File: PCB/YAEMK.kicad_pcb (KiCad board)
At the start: 2 copper layers, 165.8 x 130.8 mm, 222 parts, among them J1 DBG, P1 PC, P2 Link, P3 SSD1107, Q1 MMUN2133LT1G, Q2 DMMT5401, Q3 AO3401A, SW1 ALPS EC11, U1 24LC64, U2 SSP6206, U3 USBLC6-2SC6, U4 USBLC6-2SC6, U5 STM32F303CCTx

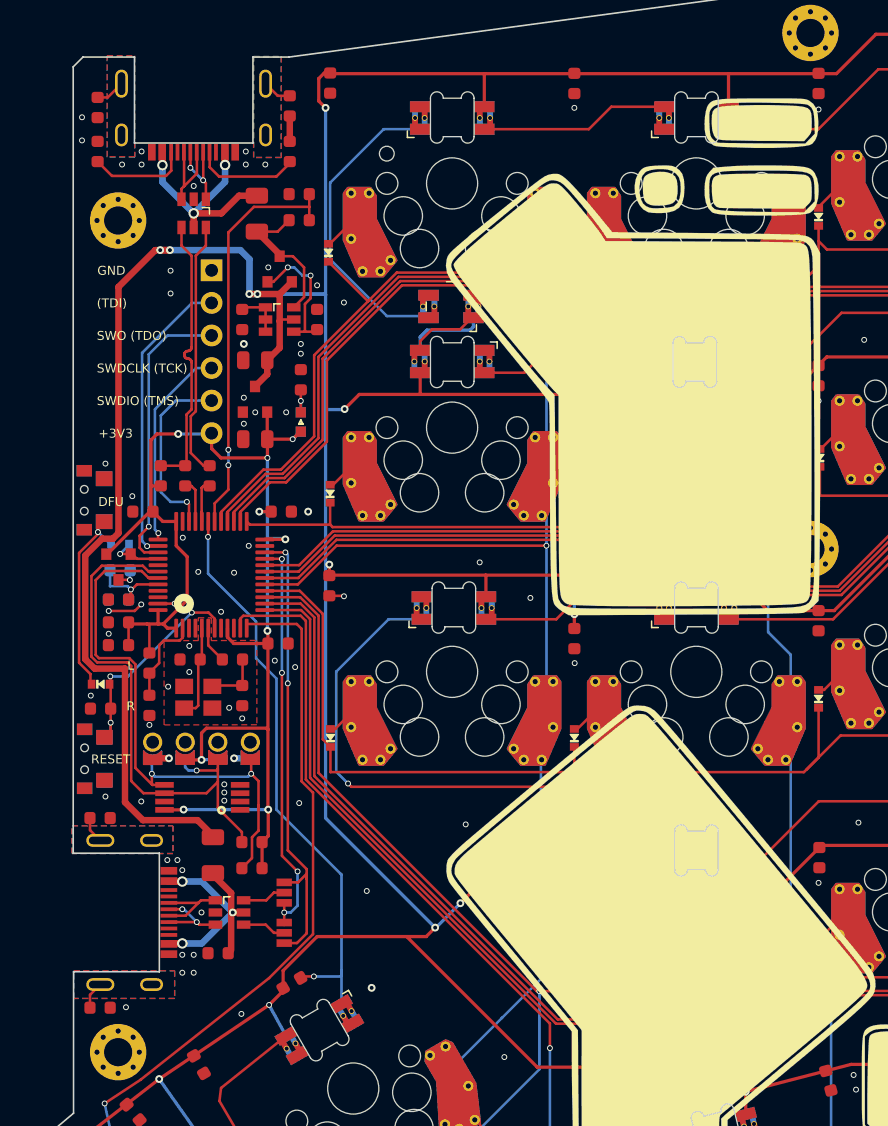
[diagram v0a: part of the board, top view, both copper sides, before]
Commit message: Update Reset / DFU circut to single button version
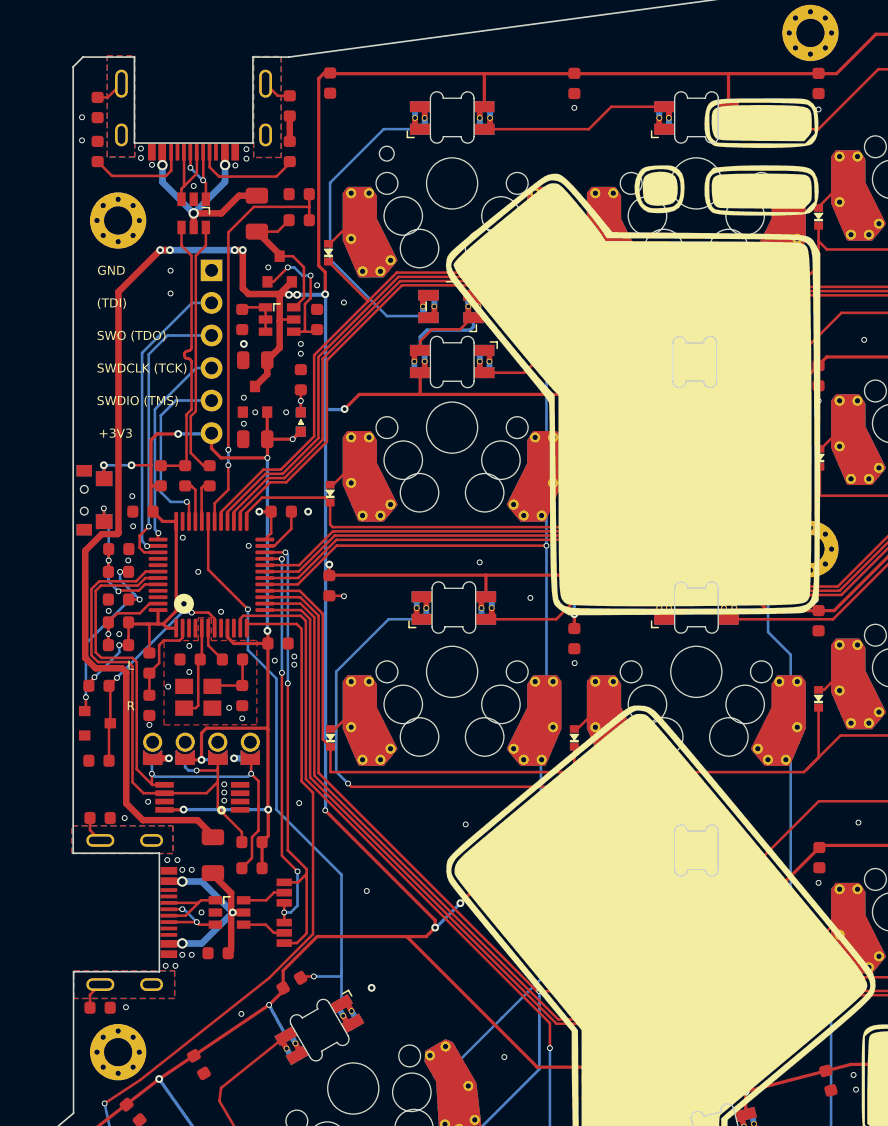
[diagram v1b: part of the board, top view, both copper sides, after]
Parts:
- removed D68, D69: 1N4148, prettylib:D_SOD-523
- removed S33: RESET, prettylib:SMD_Tacticle_Switch_TS24CA_flipable
- added R27: 100k, prettylib:SMD-0603, F.Cu at (80.6, 77.9)
- C40: value 100n -> 10u
- C42: value 100n -> 1u
- Q1: value MMUN2133LT1G -> 2N7002
- R11: value 220 -> 10k; moved to F.Cu
- R14: value 1M -> 10k; moved to F.Cu
- S32: value DFU -> RESET + DFU
- moved C42 12.7 mm to (79.1, 90.4), turned to 180 degrees
- moved Q1 12.3 mm to (79.0, 87.5), turned to 0 degrees
- moved C40 10.8 mm to (80.6, 75.7)
- moved R14 6.90 mm to (79.1, 84.6), turned to 0 degrees
- moved R11 1.65 mm to (80.7, 73.9), turned to 0 degrees
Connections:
- C40 pad 1: VSS -> BOOT0
- C40 pad 2: NRST -> Net-(C40-Pad2)
- C42 pad 1: VSS -> NRST
- C42 pad 2: BOOT0 -> VSS
- Q1 pad 1: BOOT0_CHARGE -> Net-(C40-Pad2)
- Q1 pad 2: VDD -> VSS
- Q1 pad 3: Net-(Q1-Pad3) -> NRST
- R11 pad 1: Net-(Q1-Pad3) -> BOOT0
- R11 pad 2: BOOT0 -> VSS
- R14 pad 1: BOOT0 -> VDD
- R14 pad 2: VSS -> NRST
- S32 pad 1: Net-(D68-Pad1) -> BOOT0
- S32 pad 2: VSS -> VDD
- U5 pad 40: BOOT0_CHARGE -> (no net)
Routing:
- net Net-(D68-Pad1): track 16.6 -> 0.00 mm, vias 1 -> 0
- net Net-(C40-Pad2): track 0.00 -> 15.0 mm, vias 0 -> 3
- net BOOT0: track 6.79 -> 16.3 mm, vias 1 -> 3
- net VSS: track 14.5 -> 19.9 mm
- net VDD: track 110.0 -> 114.3 mm, vias 9 -> 12
- net BOOT0_CHARGE: track 4.22 -> 0.00 mm, vias 1 -> 0
- net RGB_VDD: track 1003.6 -> 1000.7 mm, vias 29 -> 32
- net Net-(Q1-Pad3): track 1.54 -> 0.00 mm, vias 1 -> 0
- net Row2: track 153.4 -> 154.6 mm
- net I2C1_SCL: track 42.5 -> 41.5 mm
- net I2C1_SDA: track 45.1 -> 44.1 mm
- net NRST: track 17.3 -> 17.5 mm, vias 3 -> 2
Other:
- board text removed: "DFU"
- board text removed: "RESET"

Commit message: Update Gerbers
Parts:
- moved Q1 0.11 mm to (79.1, 87.5)
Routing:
- net VSS: vias 112 -> 114

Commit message: Update Plugdetect Values
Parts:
- R16: value 100k -> 10k
- R22: value 100k -> 47k
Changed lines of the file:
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@@
     (add_net "Net-(F1-Pad1)")
     (add_net "Net-(P1-PadA5)")
+    (add_net "Net-(P1-PadA8)")
     (add_net "Net-(P1-PadB5)")
+    (add_net "Net-(P1-PadB8)")
     (add_net "Net-(P1-PadS1)")
+    (add_net "Net-(P2-PadA5)")
+    (add_net "Net-(P2-PadA8)")
+    (add_net "Net-(P2-PadB5)")
+    (add_net "Net-(P2-PadB8)")
     (add_net "Net-(P2-PadS1)")
     (add_net "Net-(Q2-Pad1)")
@@
     (add_net "Net-(R18-Pad2)")
     (add_net "Net-(R19-Pad2)")
+    (add_net "Net-(U5-Pad10)")
+    (add_net "Net-(U5-Pad3)")
+    (add_net "Net-(U5-Pad4)")
+    (add_net "Net-(U5-Pad40)")
+    (add_net "Net-(U5-Pad41)")
+    (add_net "Net-(U5-Pad45)")
+    (add_net "Net-(U5-Pad46)")
     (add_net PLUG_DETECT)
     (add_net RGB_DATA)
@@
       (effects (font (size 1 1) (thickness 0.15)))
     )
-    (fp_text value 100k (at 0 1.43 90) (layer F.Fab) hide
+    (fp_text value 10k (at 0 1.43 90) (layer F.Fab) hide
       (effects (font (size 1 1) (thickness 0.15)))
     )
@@
       (effects (font (size 1 1) (thickness 0.15)))
     )
-    (fp_text value 100k (at 0 1.43) (layer F.Fab) hide
+    (fp_text value 47k (at 0 1.43) (layer F.Fab) hide
       (effects (font (size 1 1) (thickness 0.15)))
     )

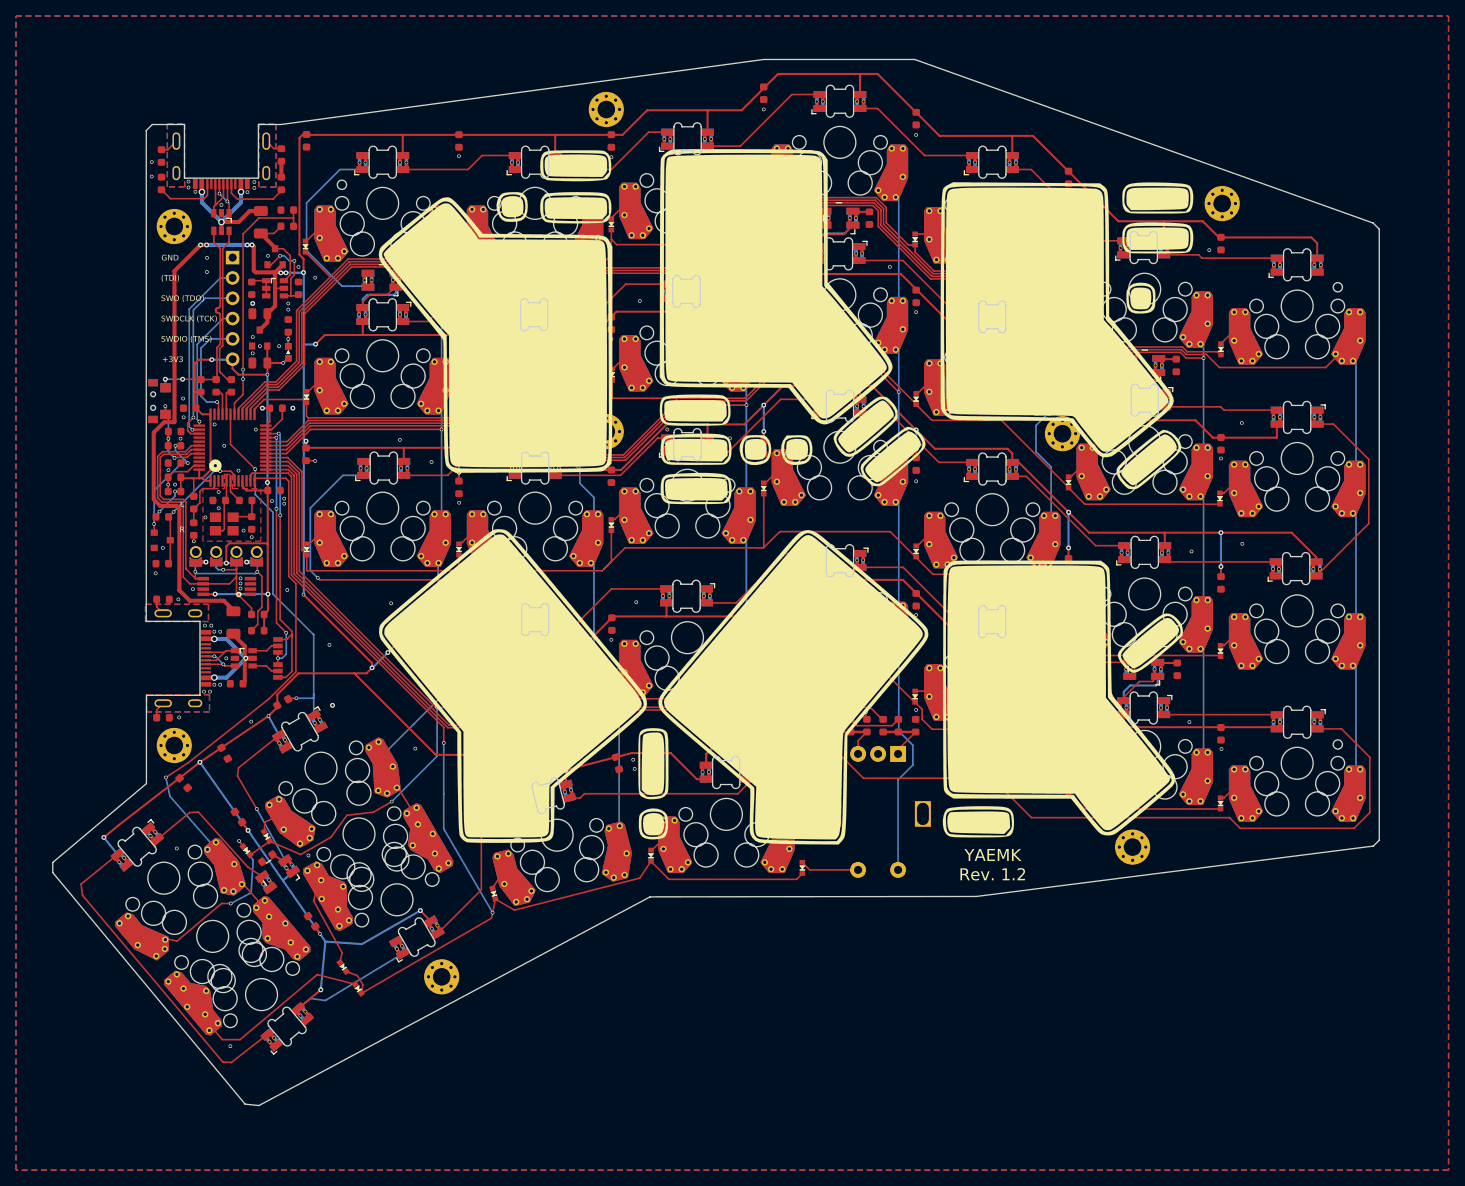
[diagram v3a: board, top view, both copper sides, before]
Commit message: Add opamp ideal diode
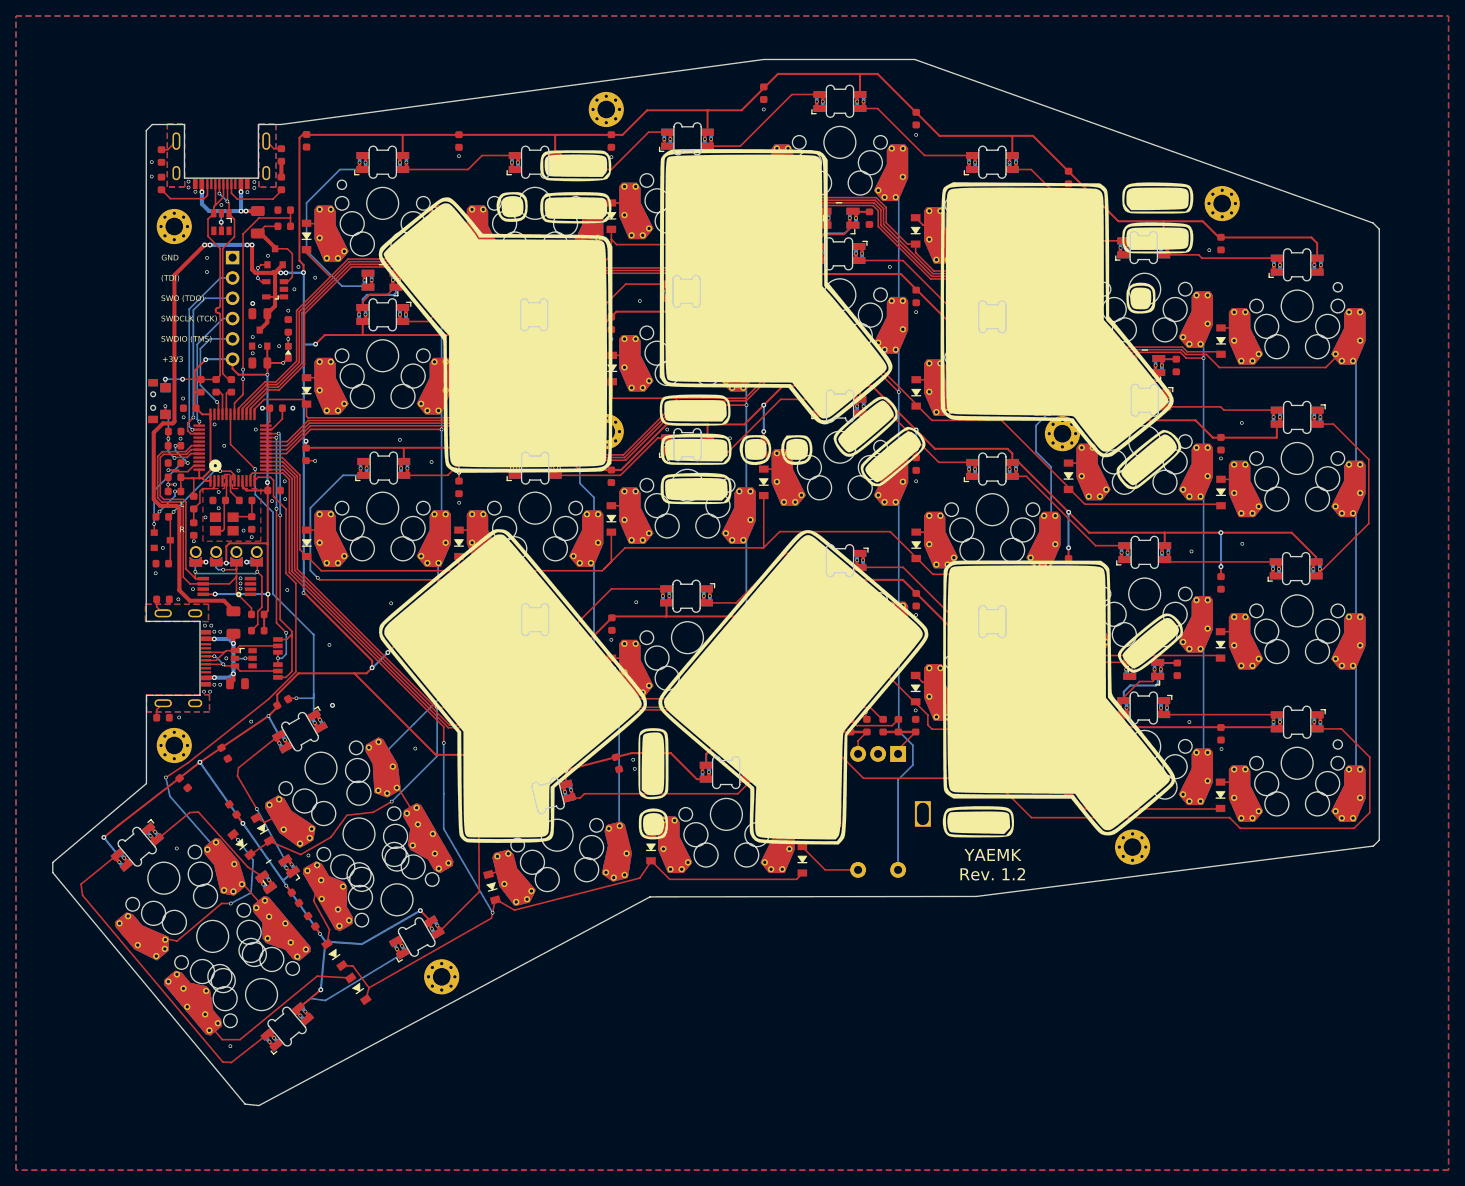
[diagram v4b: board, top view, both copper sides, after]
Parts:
- removed Q2: DMMT5401, prettylib:SOT-23-6
- removed R15: 100k, prettylib:SMD-0603
- removed R16: 10k, prettylib:SMD-0603
- added U6: LMV321, prettylib:SOT-23-5, F.Cu at (93.2, 56.1)
- C45: value 100n -> 10u; footprint prettylib:SMD-0603 -> prettylib:SMD-0805
- D1, D10, D11, D12, D13, D14, D15, D16, D17, D18, D19, D2, D20, D21, D22, D23, D24, D25, D26, D27, D28, D29, D3, D30, D31, D32, D33, D34, D4, D5, D6, D7, D8, D9: footprint prettylib:D_SOD-523 -> prettylib:D_SOD-123
- R22: value 47k -> 100k
- R23: value 100k -> 200k
- U3, U4: value USBLC6-2SC6 -> USBLC6-4SC6
- moved C53 6.07 mm to (95.8, 132.2), turned to 305 degrees
- moved D7 1.87 mm to (100.6, 139.3)
- moved D3 1.28 mm to (97.2, 49.5)
- moved C27 1.18 mm to (87.9, 121.2)
- moved D23 1.08 mm to (173.3, 48.8)
- moved D18 1.02 mm to (154.3, 42.2)
- moved D6 1.02 mm to (91.7, 123.6)
- moved D26 1.02 mm to (173.3, 106.0)
- moved D16 1.02 mm to (135.3, 103.9)
- moved D30 1.02 mm to (192.4, 117.3)
- moved D31 1.02 mm to (211.5, 62.6)
- moved D34 1.02 mm to (211.4, 119.4)
- moved D8 1.02 mm to (116.2, 49.7)
- moved D13 1.02 mm to (135.3, 47.0)
- moved D27 1.02 mm to (192.4, 59.4)
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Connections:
- P1 pad A6: ESD_USB_D+ -> USB_D+
- P1 pad A7: ESD_USB_D- -> USB_D-
- P1 pad B6: ESD_USB_D+ -> USB_D+
- P1 pad B7: ESD_USB_D- -> USB_D-
- P2 pad A6: ESD_LINK+ -> LINK+
- P2 pad A7: ESD_LINK- -> LINK-
- P2 pad B6: ESD_LINK+ -> LINK+
- P2 pad B7: ESD_LINK- -> LINK-
- U3 pad 1: ESD_USB_D- -> USB_D-
- U3 pad 3: ESD_USB_D+ -> USB_D+
- U3 pad 4: USB_D+ -> (no net)
- U3 pad 6: USB_D- -> (no net)
- U4 pad 1: ESD_LINK- -> LINK-
- U4 pad 3: ESD_LINK+ -> LINK+
- U4 pad 4: LINK+ -> (no net)
- U4 pad 6: LINK- -> (no net)
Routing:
- net USB_D+: track 21.7 -> 31.3 mm
- net USB_D-: track 20.0 -> 28.7 mm, vias 0 -> 2
- net LINK-: track 3.42 -> 11.9 mm
- net LINK+: track 3.43 -> 11.8 mm, vias 0 -> 2
- net ESD_USB_D+: track 7.13 -> 0.00 mm
- net Net-(Q3-Pad1): track 10.5 -> 3.89 mm
- net ESD_LINK-: track 6.66 -> 0.00 mm
- net ESD_LINK+: track 6.53 -> 0.00 mm, vias 2 -> 0
- net ESD_USB_D-: track 6.42 -> 0.00 mm, vias 2 -> 0
- net Net-(Q2-Pad1): track 3.79 -> 0.00 mm
- net USB_VBUS_IN_FUSED: track 19.9 -> 16.5 mm, vias 3 -> 5
- net Net-(D7-Pad2): track 11.2 -> 8.46 mm
- net Net-(D21-Pad2): track 6.24 -> 4.27 mm
- net USB_VBUS: track 18.9 -> 17.1 mm, vias 3 -> 5
- net Row3: track 154.4 -> 153.2 mm
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
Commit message: RC for real
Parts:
- C43, C44, C45: footprint prettylib:SMD-0805 -> prettylib:SMD-0603
- C46, C47: value 12p -> 20p
- U3, U4: value USBLC6-4SC6 -> SRV0504
- moved C45 0.83 mm to (89.3, 105.4)
- moved R22 0.52 mm to (94.2, 48.8)
- moved R23 0.52 mm to (94.2, 46.7)
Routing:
- net VSS: vias 113 -> 116
